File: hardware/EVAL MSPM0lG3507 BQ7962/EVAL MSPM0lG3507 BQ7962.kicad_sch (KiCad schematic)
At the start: 84 parts, among them J1 Conn_01x09_Socket, J10 Screw_Terminal_01x02, J11 Screw_Terminal_01x02, J12 Screw_Terminal_01x02, J13 Screw_Terminal_01x02, J14 Screw_Terminal_01x02, J15 Conn_01x02_Pin, J17 Conn_01x02_Pin, J2 Conn_02x05_Odd_Even, J3 Conn_01x04_Pin, J4 Screw_Terminal_01x02, J5 Conn_01x03_Pin, J6 Conn_01x02_Pin, J7 Screw_Terminal_01x02, J8 Screw_Terminal_01x02, J9 Screw_Terminal_01x02, SW1 SW_Push, U2 MCU-MSM0G3507SPM, U3 TPS62A02ADRL

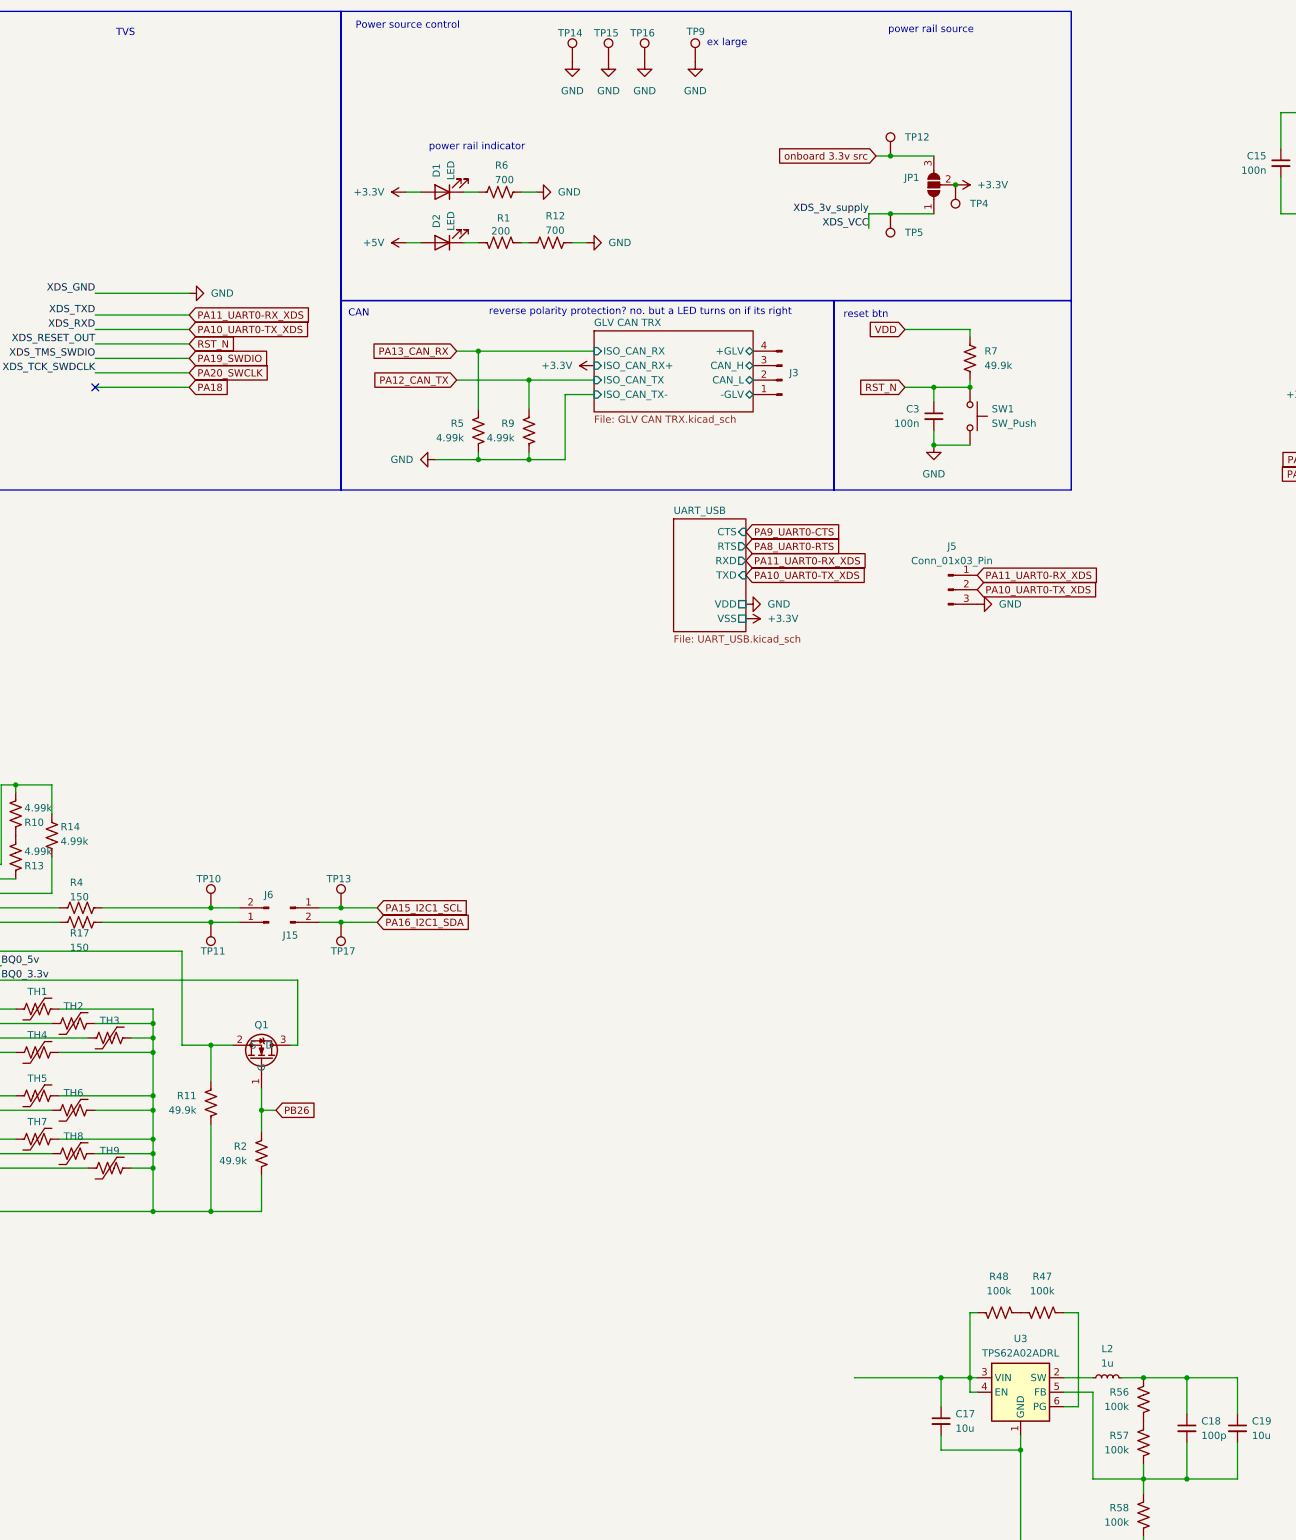
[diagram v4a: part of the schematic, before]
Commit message: ti once again making the most convenient IC's around
new TVS solution. use the
TPD4E05U06DQA
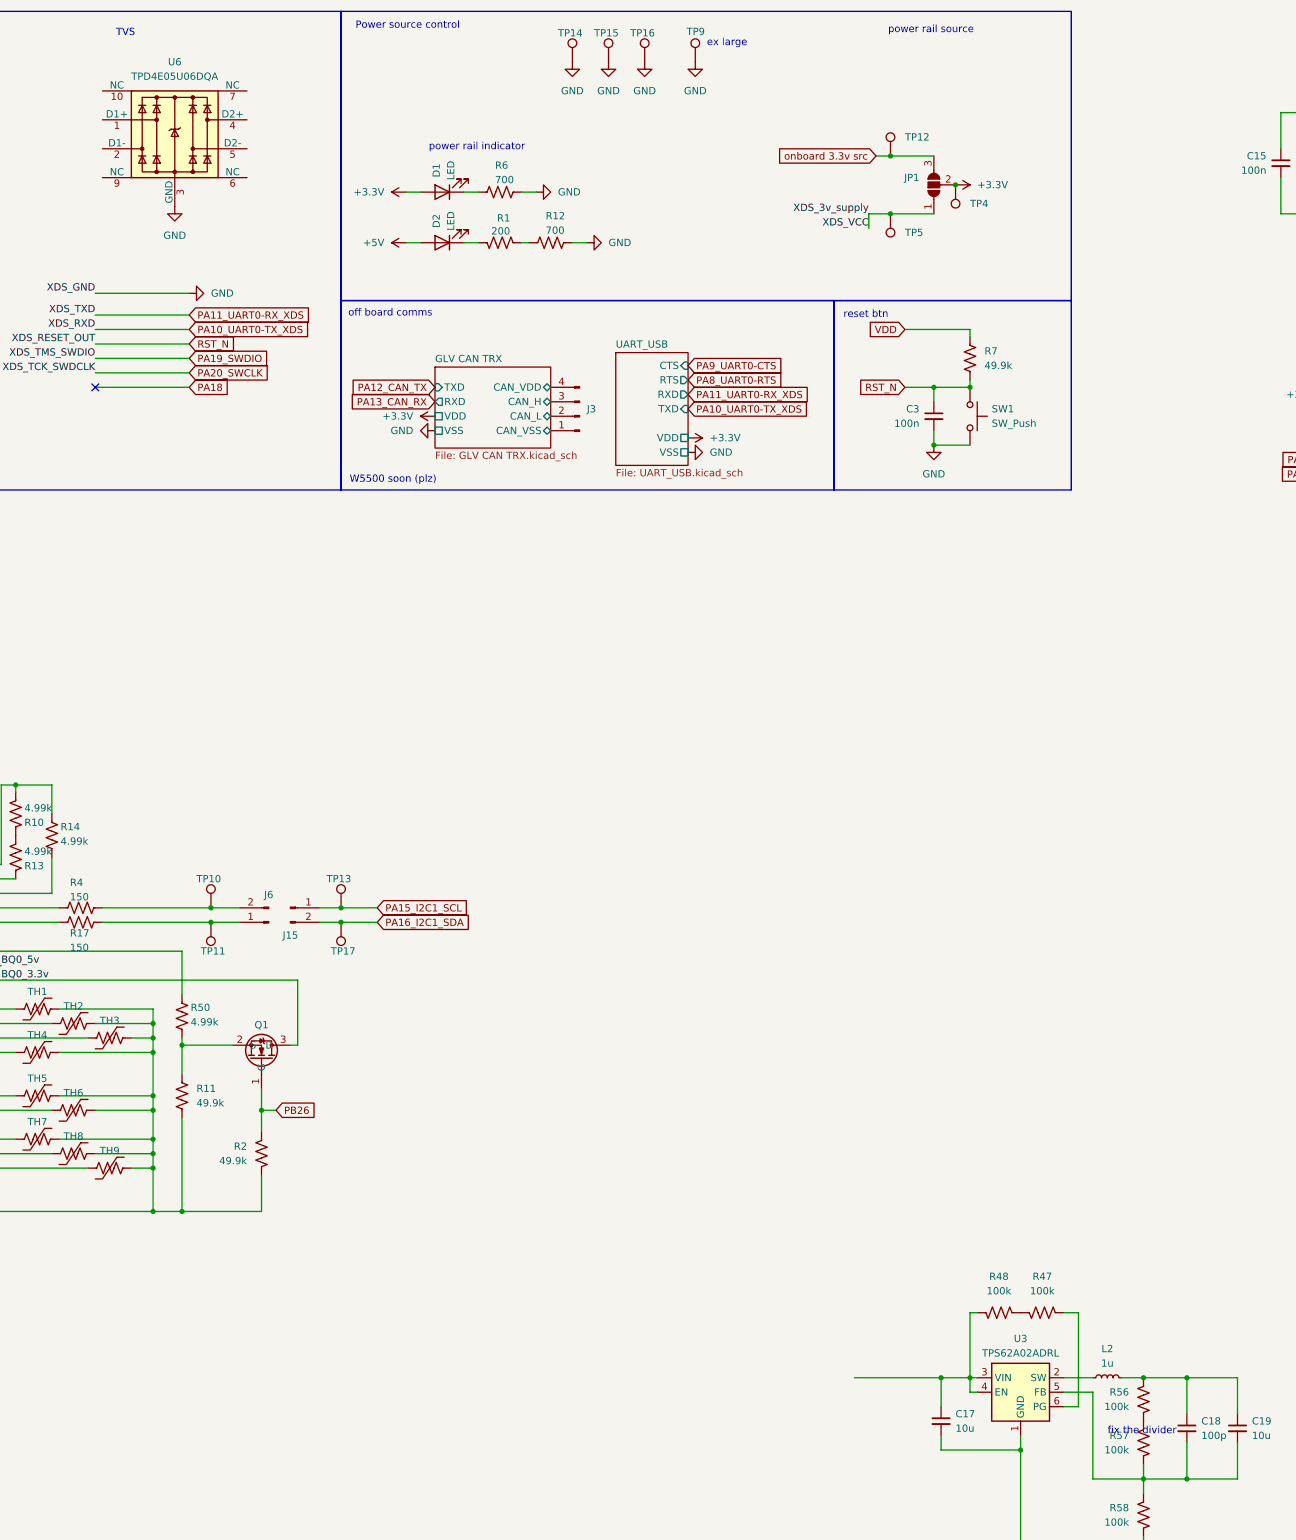
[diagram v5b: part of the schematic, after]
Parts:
- removed J5: Conn_01x03_Pin, Connector_PinHeader_2.54mm:PinHeader_1x03_P2.54mm_Vertical, symbol Connector:Conn_01x03_Pin
- removed R5, R9: 4.99k, Resistor_SMD:R_1206_3216Metric_Pad1.30x1.75mm_HandSolder, symbol Device:R_US
- added R50: 4.99k, Resistor_SMD:R_1206_3216Metric_Pad1.30x1.75mm_HandSolder, symbol Device:R_US
- added U6: TPD4E05U06DQA, Package_SON:USON-10_2.5x1.0mm_P0.5mm, symbol Power_Protection:TPD4E05U06DQA
- Q1: unit x10 (none) -> 0.052
- R10, R13, R14, R16, R18: unit x10 (none) -> 0.017
- R17, R4: unit x10 (none) -> 0.032
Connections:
- net BQ76952 16C/RST_SHUT: now also R50.1; no longer Q1.2 (S), R11.2
- net GND: now also U6.3 (GND), U6.8 (GND)
- net GLV CAN TRX/+GLV renamed GLV CAN TRX/CAN_VDD
- net GLV CAN TRX/-GLV renamed GLV CAN TRX/CAN_VSS
- new net: Q1.2 (S), R11.2, R50.2
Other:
- sheet GLV CAN TRX ports: added CAN_VDD, CAN_VSS, RXD, TXD, VDD, VSS; removed +GLV, -GLV, ISO_CAN_RX, ISO_CAN_RX+, ISO_CAN_TX, ISO_CAN_TX-
- note added: "W5500 soon (plz)"
- note added: "fix the divider"
- note added: "off board comms"
- note removed: "CAN"
- note removed: "reverse polarity protection? no. but a LED turns on if its right"
- moved on the sheet: J3, R11

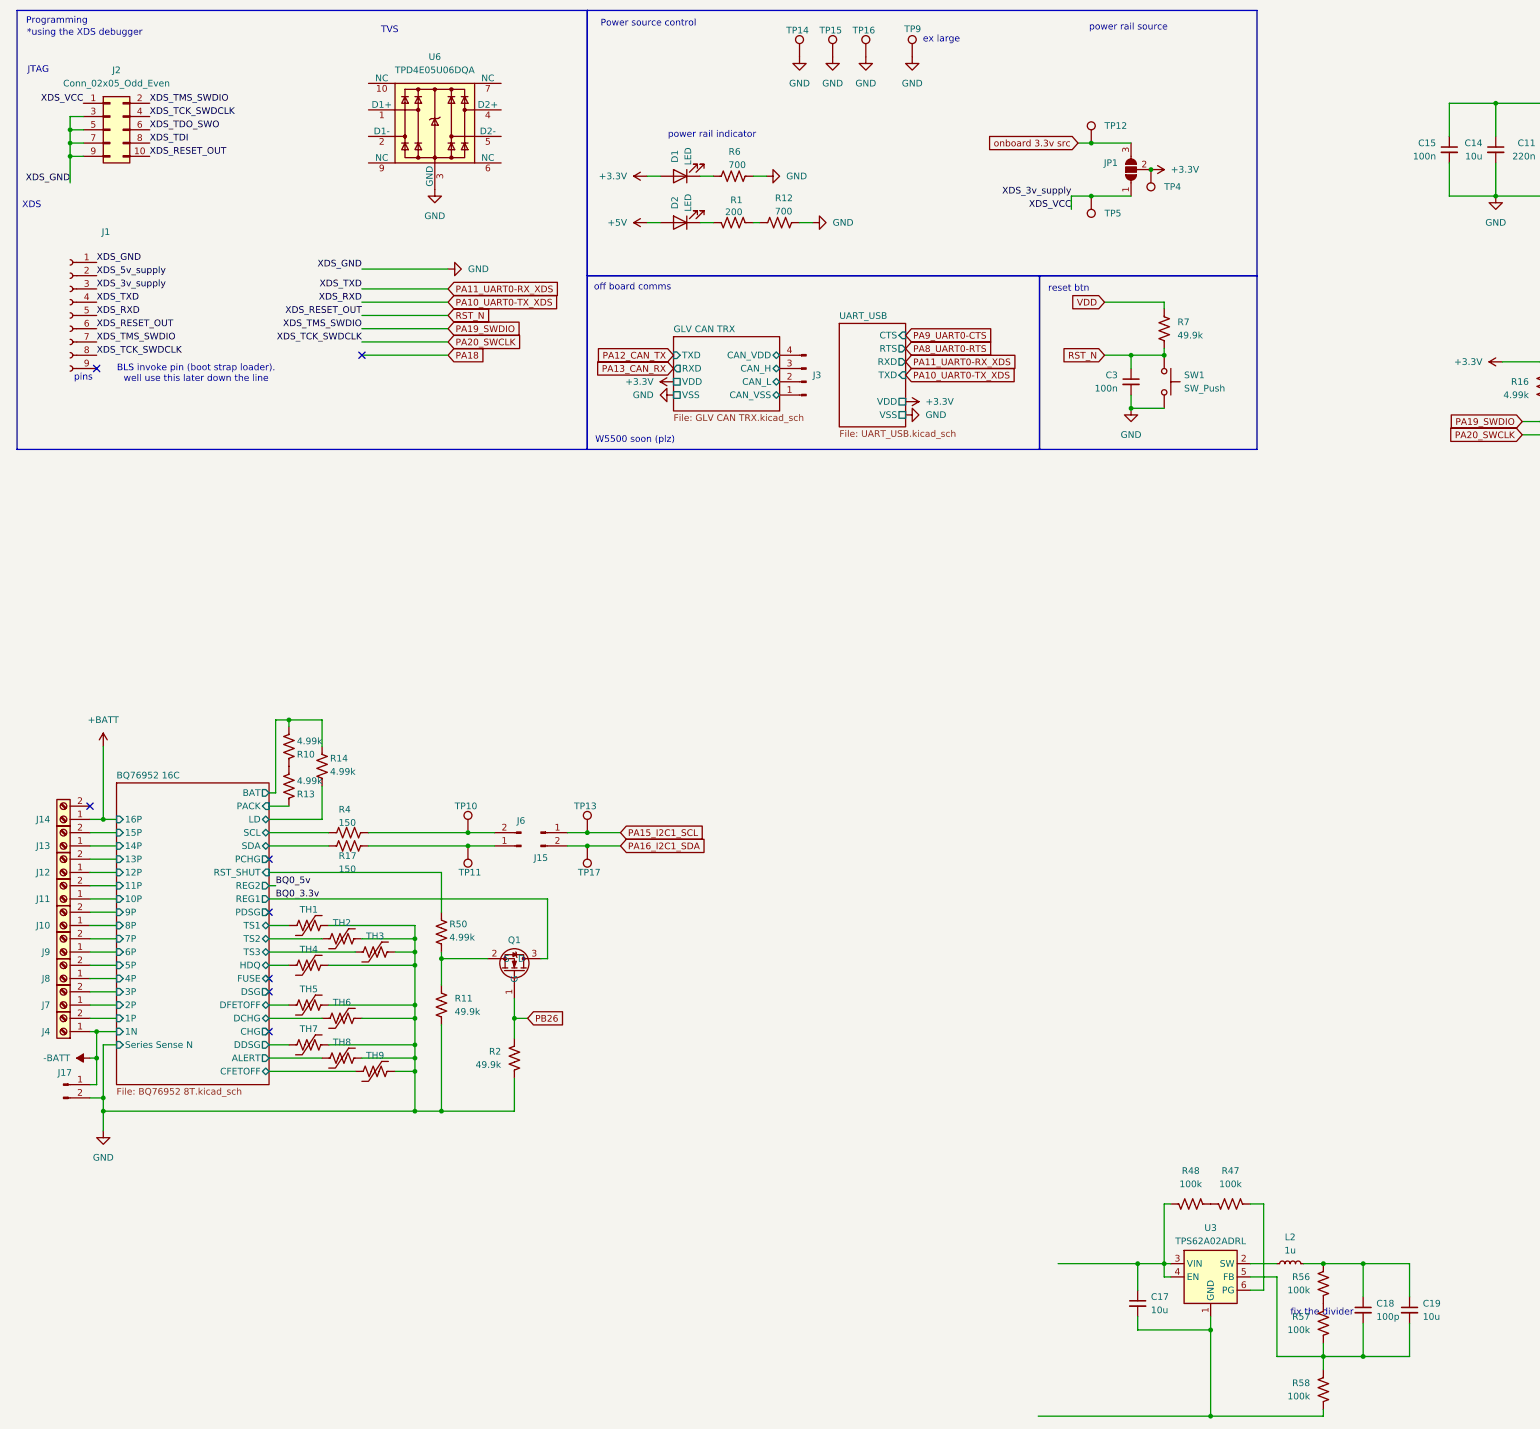
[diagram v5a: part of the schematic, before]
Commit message: corrected mosfet choice and started jumper board with xds110
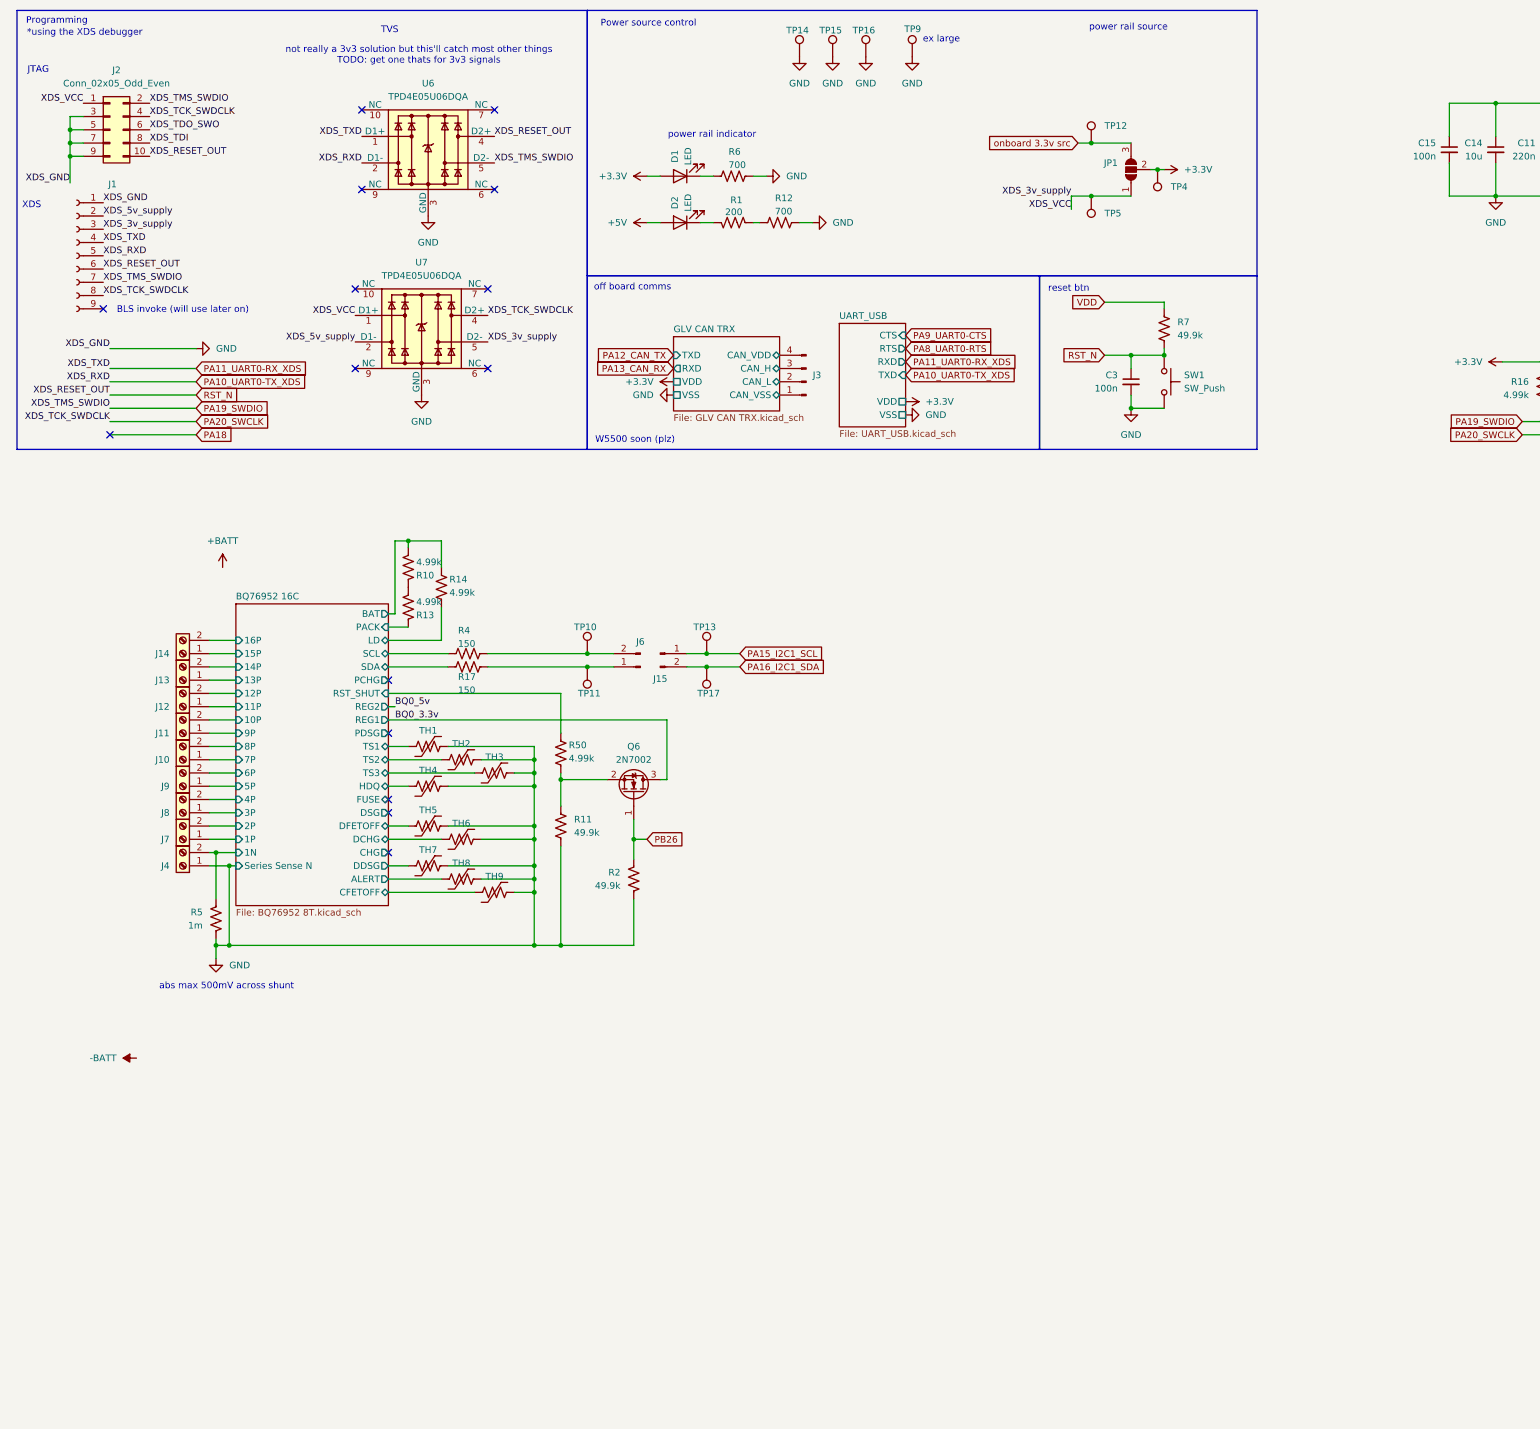
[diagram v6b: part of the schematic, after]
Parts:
- removed C17, C19: 10u, Capacitor_SMD:C_1206_3216Metric_Pad1.33x1.80mm_HandSolder, symbol Device:C_Small
- removed C18: 100p, Capacitor_SMD:C_1206_3216Metric_Pad1.33x1.80mm_HandSolder, symbol Device:C_Small
- removed J17: Conn_01x02_Pin, Connector_PinHeader_2.54mm:PinHeader_1x02_P2.54mm_Vertical, symbol Connector:Conn_01x02_Pin
- removed L2: 1u, Inductor_SMD:L_0805_2012Metric_Pad1.15x1.40mm_HandSolder, symbol Device:L_Small
- removed Q1: ~, zzLocalLibraries-Footprints:SOT8001, symbol zzLocalLibrary:NX138BKHH
- removed R47, R48, R56, R57, R58: 100k, Resistor_SMD:R_1206_3216Metric_Pad1.30x1.75mm_HandSolder, symbol Device:R_US
- removed U3: TPS62A02ADRL, Package_TO_SOT_SMD:SOT-563, symbol Regulator_Switching:TPS62A02ADRL
- added Q6: 2N7002, Package_TO_SOT_SMD:SOT-23, symbol Transistor_FET:2N7002
- added R5: 1m, zzLocalLibraries-Footprints:R_shunt_3921, symbol Device:R_US
- added U7: TPD4E05U06DQA, Package_SON:USON-10_2.5x1.0mm_P0.5mm, symbol Power_Protection:TPD4E05U06DQA
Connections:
- net +BATT: no longer J14.1 (Pin_1)
- net -BATT: no longer J4.1 (Pin_1)
- net BQ0_3.3v: now also Q6.3 (D)
- net BQ76952 16C/10P: now also J11.2 (Pin_2); no longer J11.1 (Pin_1)
- net BQ76952 16C/11P: now also J12.1 (Pin_1); no longer J11.2 (Pin_2)
- net BQ76952 16C/12P: now also J12.2 (Pin_2); no longer J12.1 (Pin_1)
- net BQ76952 16C/13P: now also J13.1 (Pin_1); no longer J12.2 (Pin_2)
- net BQ76952 16C/14P: now also J13.2 (Pin_2); no longer J13.1 (Pin_1)
- net BQ76952 16C/15P: now also J14.1 (Pin_1); no longer J13.2 (Pin_2)
- net BQ76952 16C/1P: now also J7.1 (Pin_1); no longer J4.2 (Pin_2)
- net BQ76952 16C/2P: now also J7.2 (Pin_2); no longer J7.1 (Pin_1)
- net BQ76952 16C/3P: now also J8.1 (Pin_1); no longer J7.2 (Pin_2)
- net BQ76952 16C/4P: now also J8.2 (Pin_2); no longer J8.1 (Pin_1)
- net BQ76952 16C/5P: now also J9.1 (Pin_1); no longer J8.2 (Pin_2)
- net BQ76952 16C/6P: now also J9.2 (Pin_2); no longer J9.1 (Pin_1)
- net BQ76952 16C/7P: now also J10.1 (Pin_1); no longer J9.2 (Pin_2)
- net BQ76952 16C/8P: now also J10.2 (Pin_2); no longer J10.1 (Pin_1)
- net BQ76952 16C/9P: now also J11.1 (Pin_1); no longer J10.2 (Pin_2)
- net GND: now also J4.1 (Pin_1), R5.1, U7.3 (GND), U7.8 (GND)
- net PA10_UART0-TX_XDS: now also U6.2 (D1-)
- net PA11_UART0-RX_XDS: now also U6.1 (D1+)
- net PA19_SWDIO: now also U6.5 (D2-)
- net PA20_SWCLK: now also U7.4 (D2+)
- net PB26: now also Q6.1 (G)
- net RST_N: now also U6.4 (D2+)
- net XDS_3v_supply: now also U7.1 (D1+), U7.5 (D2-)
- net XDS_5v_supply: now also U7.2 (D1-)
- net BQ76952 16C/16P: now reaches J14.2 (Pin_2)
- net at R11.2, R50.2: now also Q6.2 (S)
- new net BQ76952 16C/1N: J4.2 (Pin_2), R5.2
- no-connect marks 43 -> 50
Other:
- note added: "BLS invoke (will use later on)"
- note added: "abs max 500mV across shunt"
- note added: "not really a 3v3 solution but this'll catch most other things TODO: get one thats for 3v3 signals"
- note removed: "BLS invoke pin (boot strap loader). well use this later down the line"
- note removed: "fix the divider"
- note removed: "pins"
- moved on the sheet: J1, J10, J11, J12, J13, J14, J15, J4, J6, J7, J8, J9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
